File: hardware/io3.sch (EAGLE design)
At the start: 37 parts, among them IC2 74HC14D, IC3 74HC74D, Q1 BC857BSMD, U1 TXB0108PWR

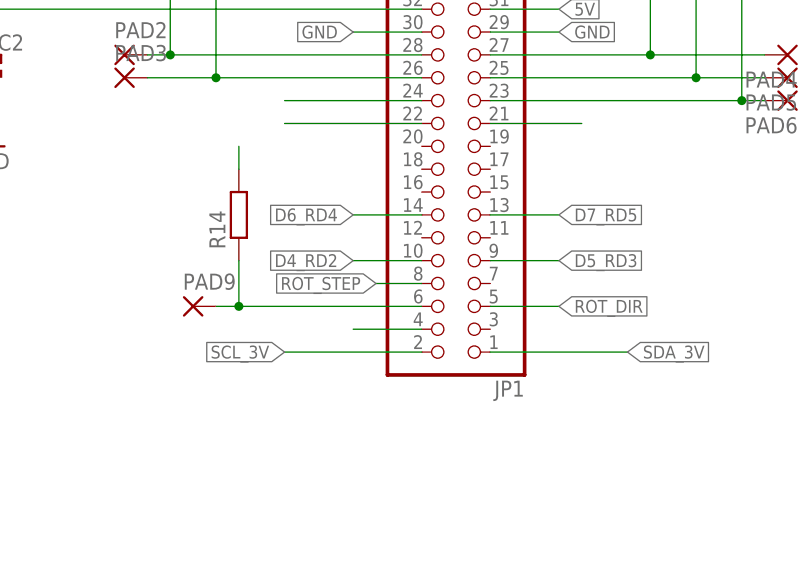
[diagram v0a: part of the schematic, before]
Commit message: io3 board fix - no need to twist lines in ribbon
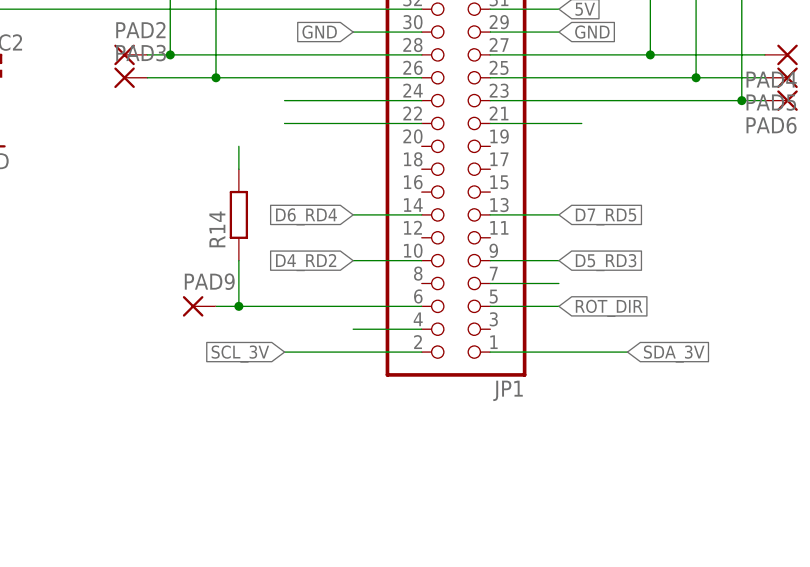
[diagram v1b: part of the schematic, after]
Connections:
- net ROT_STEP: now also JP1.7; no longer JP1.8
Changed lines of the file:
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@@
 </segment>
 <segment>
-<pinref part="JP1" gate="A" pin="8"/>
-<wire x1="177.8" y1="170.18" x2="172.72" y2="170.18" width="0.1524" layer="91"/>
-<label x="172.72" y="170.18" size="1.4224" layer="95" rot="R180" xref="yes"/>
+<pinref part="JP1" gate="A" pin="7"/>
+<wire x1="185.42" y1="170.18" x2="193.04" y2="170.18" width="0.1524" layer="91"/>
 </segment>
 </net>
